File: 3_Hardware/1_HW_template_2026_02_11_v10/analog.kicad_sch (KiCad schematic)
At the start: 8 parts, among them U6 MCP6002-xSN, Y1 ${SIM.PARAMS}

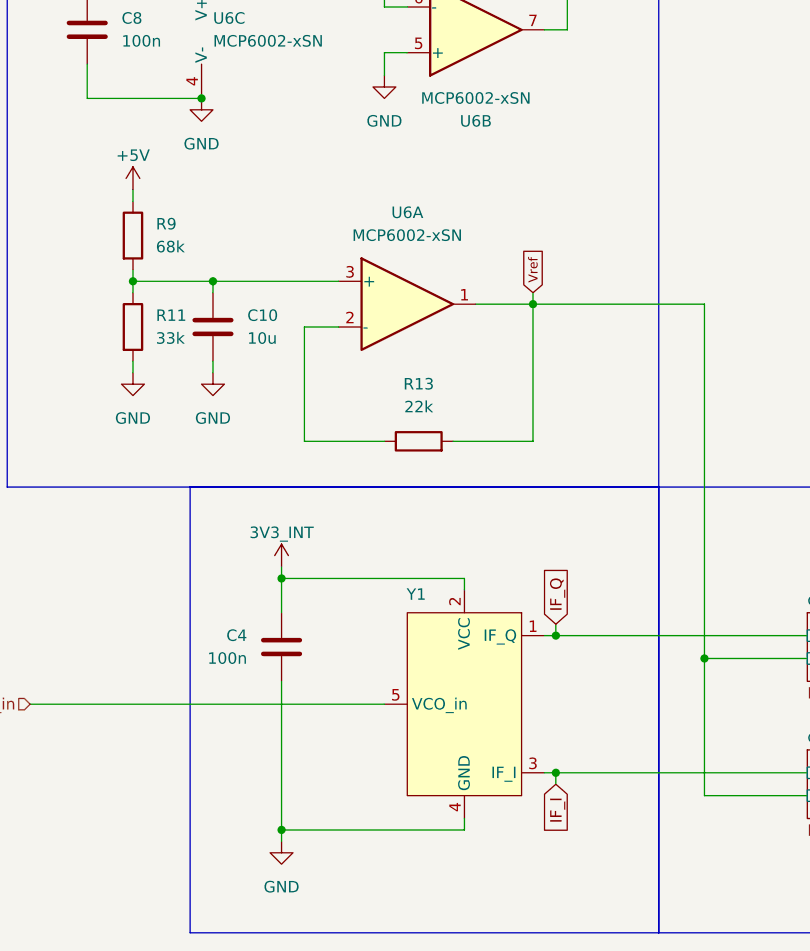
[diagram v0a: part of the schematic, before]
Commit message: added amp filter v5
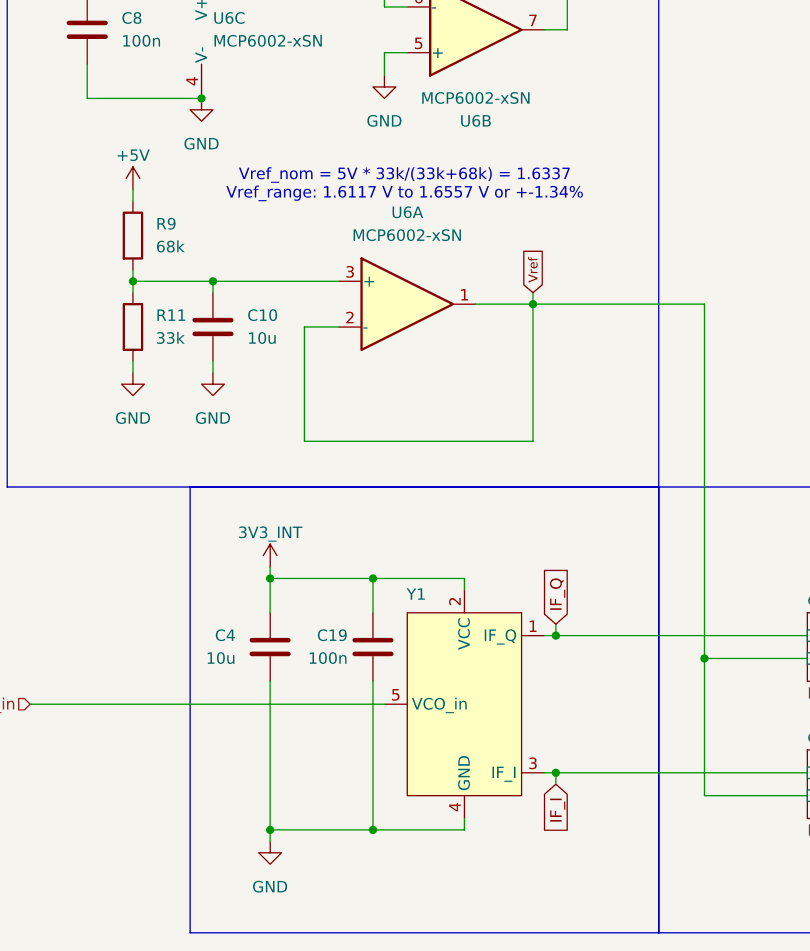
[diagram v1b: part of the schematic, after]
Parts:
- removed R13: 22k, Resistor_SMD:R_0805_2012Metric_Pad1.20x1.40mm_HandSolder, symbol Device:R
- added C19: 100n, Capacitor_SMD:C_0805_2012Metric_Pad1.18x1.45mm_HandSolder, symbol Device:C
- C4: value 100n -> 10u
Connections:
- net 3V3_INT: now also C19.1
- net GND: now also C19.2
- net Vref: now also U6.2 (-)
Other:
- note added: "Vref_nom = 5V * 33k/(33k+68k) = 1.6337 Vref_range: 1.6117 V to 1.6557 V or +-1.34%"
- moved on the sheet: C4
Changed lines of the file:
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@@
+		)
+	)
+	(text "Vref_nom = 5V * 33k/(33k+68k) = 1.6337\nVref_range: 1.6117 V to 1.6557 V or +-1.34%"
+		(exclude_from_sim no)
+		(at 70.866 52.832 0)
+		(effects
+			(font
+				(size 1.27 1.27)
+			)
 		)
 	)
@@
 	)
 	(junction
-		(at 57.15 96.52)
+		(at 67.31 96.52)
 		(diameter 0)
 		(color 0 0 0 0)
@@
 	)
 	(junction
-		(at 57.15 124.46)
+		(at 55.88 124.46)
+		(diameter 0)
+		(color 0 0 0 0)
+	)
+	(junction
+		(at 55.88 96.52)
 		(diameter 0)
 		(color 0 0 0 0)
@@
 	)
 	(junction
+		(at 67.31 124.46)
+		(diameter 0)
+		(color 0 0 0 0)
+	)
+	(junction
 		(at 87.63 118.11)
 		(diameter 0)
@@
 	(wire
 		(pts
+			(xy 55.88 96.52) (xy 67.31 96.52)
+		)
+		(stroke
+			(width 0)
+			(type default)
+		)
+	)
+	(wire
+		(pts
 			(xy 40.64 53.34) (xy 40.64 54.61)
 		)
@@
 	(wire
 		(pts
+			(xy 67.31 107.95) (xy 67.31 124.46)
+		)
+		(stroke
+			(width 0)
+			(type default)
+		)
+	)
+	(wire
+		(pts
 			(xy 88.9 27.94) (xy 88.9 35.56)
 		)
@@
 	(wire
 		(pts
-			(xy 76.2 81.28) (xy 85.09 81.28)
-		)
-		(stroke
-			(width 0)
-			(type default)
-		)
-	)
-	(wire
-		(pts
 			(xy 29.21 110.49) (xy 68.58 110.49)
 		)
@@
 	(wire
 		(pts
+			(xy 55.88 124.46) (xy 67.31 124.46)
+		)
+		(stroke
+			(width 0)
+			(type default)
+		)
+	)
+	(wire
+		(pts
 			(xy 85.09 64.77) (xy 85.09 66.04)
 		)
@@
 	(wire
 		(pts
+			(xy 67.31 96.52) (xy 77.47 96.52)
+		)
+		(stroke
+			(width 0)
+			(type default)
+		)
+	)
+	(wire
+		(pts
 			(xy 71.12 33.02) (xy 68.58 33.02)
 		)
@@
 	(wire
 		(pts
-			(xy 59.69 81.28) (xy 68.58 81.28)
+			(xy 59.69 81.28) (xy 85.09 81.28)
 		)
 		(stroke
@@
 	(wire
 		(pts
+			(xy 67.31 96.52) (xy 67.31 100.33)
+		)
+		(stroke
+			(width 0)
+			(type default)
+		)
+	)
+	(wire
+		(pts
 			(xy 40.64 63.5) (xy 40.64 64.77)
 		)
@@
 	(wire
 		(pts
-			(xy 57.15 124.46) (xy 57.15 125.73)
+			(xy 55.88 124.46) (xy 55.88 125.73)
 		)
 		(stroke
@@
 	(wire
 		(pts
-			(xy 57.15 96.52) (xy 57.15 100.33)
+			(xy 55.88 96.52) (xy 55.88 100.33)
 		)
 		(stroke
@@
 	(wire
 		(pts
-			(xy 57.15 96.52) (xy 77.47 96.52)
-		)
-		(stroke
-			(width 0)
-			(type default)
-		)
-	)
-	(wire
-		(pts
 			(xy 35.56 39.37) (xy 35.56 43.18)
 		)
@@
 	(wire
 		(pts
+			(xy 67.31 124.46) (xy 77.47 124.46)
+		)
+		(stroke
+			(width 0)
+			(type default)
+		)
+	)
+	(wire
+		(pts
 			(xy 104.14 120.65) (xy 104.14 105.41)
 		)
@@
 	(wire
 		(pts
-			(xy 57.15 107.95) (xy 57.15 124.46)
+			(xy 55.88 107.95) (xy 55.88 124.46)
 		)
 		(stroke
@@
 	(wire
 		(pts
-			(xy 57.15 124.46) (xy 77.47 124.46)
-		)
-		(stroke
-			(width 0)
-			(type default)
-		)
-	)
-	(wire
-		(pts
 			(xy 87.63 118.11) (xy 115.57 118.11)
 		)
@@
 	(wire
 		(pts
-			(xy 57.15 95.25) (xy 57.15 96.52)
+			(xy 55.88 95.25) (xy 55.88 96.52)
 		)
 		(stroke
@@
 	)
 	(symbol
-		(lib_id "Device:R")
-		(at 72.39 81.28 90)
+		(lib_id "Device:C")
+		(at 67.31 104.14 0)
+		(mirror y)
 		(unit 1)
 		(exclude_from_sim no)
@@
 		(on_board yes)
 		(dnp no)
-		(fields_autoplaced yes)
-		(property "Reference" "R13"
-			(at 72.39 74.93 90)
-			(effects
-				(font
-					(size 1.27 1.27)
-				)
-			)
-		)
-		(property "Value" "22k"
-			(at 72.39 77.47 90)
-			(effects
-				(font
-					(size 1.27 1.27)
-				)
-			)
-		)
-		(property "Footprint" "Resistor_SMD:R_0805_2012Metric_Pad1.20x1.40mm_HandSolder"
-			(at 72.39 83.058 90)
+		(property "Reference" "C19"
+			(at 64.516 102.87 0)
+			(effects
+				(font
+					(size 1.27 1.27)
+				)
+				(justify left)
+			)
+		)
+		(property "Value" "100n"
+			(at 64.516 105.41 0)
+			(effects
+				(font
+					(size 1.27 1.27)
+				)
+				(justify left)
+			)
+		)
+		(property "Footprint" "Capacitor_SMD:C_0805_2012Metric_Pad1.18x1.45mm_HandSolder"
+			(at 66.3448 107.95 0)
 			(effects
 				(font
@@
 		)
 		(property "Datasheet" "~"
-			(at 72.39 81.28 0)
+			(at 67.31 104.14 0)
 			(effects
 				(font
@@
 		)
 		(property "Description" ""
-			(at 72.39 81.28 0)
+			(at 67.31 104.14 0)
 			(effects
 				(font
@@
 			(project "HW_template"
 				(path "/1f276d59-ad9b-4e70-a842-f3b7e562eb9b/53678366-9d6f-42c1-9420-188f8f258077"
-					(reference "R13")
+					(reference "C19")
 					(unit 1)
 				)
@@
 	(symbol
 		(lib_id "power:GND")
-		(at 57.15 125.73 0)
+		(at 55.88 125.73 0)
 		(mirror y)
 		(unit 1)
@@
 		(fields_autoplaced yes)
 		(property "Reference" "#PWR013"
-			(at 57.15 132.08 0)
+			(at 55.88 132.08 0)
 			(effects
 				(font
@@
 		)
 		(property "Value" "GND"
-			(at 57.15 130.81 0)
+			(at 55.88 130.81 0)
 			(effects
 				(font
@@
 		)
 		(property "Footprint" ""
-			(at 57.15 125.73 0)
+			(at 55.88 125.73 0)
 			(effects
 				(font
@@
 		)
 		(property "Datasheet" ""
-			(at 57.15 125.73 0)
+			(at 55.88 125.73 0)
 			(effects
 				(font
@@
 		)
 		(property "Description" "Power symbol creates a global label with name \"GND\" , ground"
-			(at 57.15 125.73 0)
+			(at 55.88 125.73 0)
 			(effects
 				(font
@@
 	(symbol
 		(lib_id "power:+3V0")
-		(at 57.15 95.25 0)
+		(at 55.88 95.25 0)
 		(mirror y)
 		(unit 1)
@@
 		(dnp no)
 		(property "Reference" "#PWR011"
-			(at 57.15 99.06 0)
+			(at 55.88 99.06 0)
 			(effects
 				(font
@@
 		)
 		(property "Value" "3V3_INT"
-			(at 57.15 91.44 0)
+			(at 55.88 91.44 0)
 			(effects
 				(font
@@
 		)
 		(property "Footprint" ""
-			(at 57.15 95.25 0)
+			(at 55.88 95.25 0)
 			(effects
 				(font
@@
 		)
 		(property "Datasheet" ""
-			(at 57.15 95.25 0)
+			(at 55.88 95.25 0)
 			(effects
 				(font
@@
 		)
 		(property "Description" "Power symbol creates a global label with name \"+3V0\""
-			(at 57.15 95.25 0)
+			(at 55.88 95.25 0)
 			(effects
 				(font
@@
 	(symbol
 		(lib_id "Device:C")
-		(at 57.15 104.14 0)
+		(at 55.88 104.14 0)
 		(mirror y)
 		(unit 1)
@@
 		(fields_autoplaced yes)
 		(property "Reference" "C4"
-			(at 53.34 102.8699 0)
+			(at 52.07 102.8699 0)
 			(effects
 				(font
@@
 			)
 		)
-		(property "Value" "100n"
-			(at 53.34 105.4099 0)
+		(property "Value" "10u"
+			(at 52.07 105.4099 0)
 			(effects
 				(font
@@
 		)
 		(property "Footprint" "Capacitor_SMD:C_0805_2012Metric_Pad1.18x1.45mm_HandSolder"
-			(at 56.1848 107.95 0)
+			(at 54.9148 107.95 0)
 			(effects
 				(font
@@
 		)
 		(property "Datasheet" "~"
-			(at 57.15 104.14 0)
+			(at 55.88 104.14 0)
 			(effects
 				(font
@@
 		)
 		(property "Description" ""
-			(at 57.15 104.14 0)
-			(effects
-				(font
+			(at 55.88 104.14 0)
+			(effects
+				(font

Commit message: finalize main feature
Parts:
- removed unit 2 of U6
- R11: value 33k -> 10k
- R9: value 68k -> 10k
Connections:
- net +5V is gone; now on net 3V3_INT: R9.1
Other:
- note added: "Vref_nom = 3V3 * 10k/(10k+10k) = 1.65 Vref_range: ±16.5 mV ±1%"
- note removed: "Vref_nom = 5V * 33k/(33k+68k) = 1.6337 Vref_range: 1.6117 V to 1.6557 V or +-1.34%"
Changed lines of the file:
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@@
 		)
 	)
-	(text "Vref_nom = 5V * 33k/(33k+68k) = 1.6337\nVref_range: 1.6117 V to 1.6557 V or +-1.34%"
+	(text "Vref_nom = 3V3 * 10k/(10k+10k) = 1.65\nVref_range: ±16.5 mV ±1%"
 		(exclude_from_sim no)
-		(at 70.866 52.832 0)
+		(at 73.152 52.324 0)
 		(effects
 			(font
@@
 	)
 	(junction
-		(at 85.09 66.04)
+		(at 81.28 66.04)
 		(diameter 0)
 		(color 0 0 0 0)
@@
 	(wire
 		(pts
-			(xy 85.09 81.28) (xy 85.09 66.04)
+			(xy 81.28 73.66) (xy 81.28 66.04)
 		)
 		(stroke
@@
 	(wire
 		(pts
-			(xy 88.9 27.94) (xy 88.9 35.56)
-		)
-		(stroke
-			(width 0)
-			(type default)
-		)
-	)
-	(wire
-		(pts
 			(xy 87.63 118.11) (xy 86.36 118.11)
 		)
@@
 	(wire
 		(pts
-			(xy 104.14 66.04) (xy 85.09 66.04)
-		)
-		(stroke
-			(width 0)
-			(type default)
-		)
-	)
-	(wire
-		(pts
-			(xy 68.58 27.94) (xy 88.9 27.94)
+			(xy 104.14 66.04) (xy 81.28 66.04)
 		)
 		(stroke
@@
 	(wire
 		(pts
-			(xy 85.09 64.77) (xy 85.09 66.04)
+			(xy 81.28 64.77) (xy 81.28 66.04)
 		)
 		(stroke
@@
 	(wire
 		(pts
-			(xy 71.12 33.02) (xy 68.58 33.02)
-		)
-		(stroke
-			(width 0)
-			(type default)
-		)
-	)
-	(wire
-		(pts
-			(xy 59.69 81.28) (xy 85.09 81.28)
+			(xy 59.69 73.66) (xy 81.28 73.66)
 		)
 		(stroke
@@
 	(wire
 		(pts
-			(xy 78.74 66.04) (xy 85.09 66.04)
+			(xy 78.74 66.04) (xy 81.28 66.04)
 		)
 		(stroke
@@
 	(wire
 		(pts
-			(xy 68.58 33.02) (xy 68.58 27.94)
-		)
-		(stroke
-			(width 0)
-			(type default)
-		)
-	)
-	(wire
-		(pts
 			(xy 77.47 97.79) (xy 77.47 96.52)
 		)
@@
 	(wire
 		(pts
-			(xy 59.69 68.58) (xy 59.69 81.28)
+			(xy 59.69 68.58) (xy 59.69 73.66)
 		)
 		(stroke
@@
 	(wire
 		(pts
-			(xy 68.58 38.1) (xy 71.12 38.1)
-		)
-		(stroke
-			(width 0)
-			(type default)
-		)
-	)
-	(wire
-		(pts
 			(xy 35.56 39.37) (xy 35.56 43.18)
 		)
@@
 	(wire
 		(pts
-			(xy 86.36 35.56) (xy 88.9 35.56)
-		)
-		(stroke
-			(width 0)
-			(type default)
-		)
-	)
-	(wire
-		(pts
 			(xy 87.63 101.6) (xy 87.63 102.87)
 		)
@@
 		(pts
 			(xy 49.53 72.39) (xy 49.53 73.66)
-		)
-		(stroke
-			(width 0)
-			(type default)
-		)
-	)
-	(wire
-		(pts
-			(xy 68.58 38.1) (xy 68.58 40.64)
 		)
 		(stroke
@@
 	(global_label "Vref"
 		(shape input)
-		(at 85.09 64.77 90)
+		(at 81.28 64.77 90)
 		(fields_autoplaced yes)
 		(effects
@@
 		)
 		(property "Intersheetrefs" "${INTERSHEET_REFS}"
-			(at 85.09 59.5151 90)
+			(at 81.28 59.5151 90)
 			(effects
 				(font
@@
 			)
 			(justify left)
+		)
+	)
+	(symbol
+		(lib_id "power:+3V0")
+		(at 40.64 53.34 0)
+		(unit 1)
+		(exclude_from_sim no)
+		(in_bom yes)
+		(on_board yes)
+		(dnp no)
+		(property "Reference" "#PWR014"
+			(at 40.64 57.15 0)
+			(effects
+				(font
+					(size 1.27 1.27)
+				)
+				(hide yes)
+			)
+		)
+		(property "Value" "3V3_INT"
+			(at 40.64 49.53 0)
+			(effects
+				(font
+					(size 1.27 1.27)
+				)
+			)
+		)
+		(property "Footprint" ""
+			(at 40.64 53.34 0)
+			(effects
+				(font
+					(size 1.27 1.27)
+				)
+				(hide yes)
+			)
+		)
+		(property "Datasheet" ""
+			(at 40.64 53.34 0)
+			(effects
+				(font
+					(size 1.27 1.27)
+				)
+				(hide yes)
+			)
+		)
+		(property "Description" "Power symbol creates a global label with name \"+3V0\""
+			(at 40.64 53.34 0)
+			(effects
+				(font
+					(size 1.27 1.27)
+				)
+				(hide yes)
+			)
+		)
+		(pin "1"
+		)
+		(instances
+			(project "HW_template"
+				(path "/1f276d59-ad9b-4e70-a842-f3b7e562eb9b/53678366-9d6f-42c1-9420-188f8f258077"
+					(reference "#PWR014")
+					(unit 1)
+				)
+			)
 		)
 	)
@@
 	)
 	(symbol
-		(lib_id "power:+5V")
-		(at 40.64 53.34 0)
-		(unit 1)
-		(exclude_from_sim no)
-		(in_bom yes)
-		(on_board yes)
-		(dnp no)
-		(property "Reference" "#PWR021"
-			(at 40.64 57.15 0)
-			(effects
-				(font
-					(size 1.27 1.27)
-				)
-				(hide yes)
-			)
-		)
-		(property "Value" "+5V"
-			(at 40.64 49.53 0)
-			(effects
-				(font
-					(size 1.27 1.27)
-				)
-			)
-		)
-		(property "Footprint" ""
-			(at 40.64 53.34 0)
-			(effects
-				(font
-					(size 1.27 1.27)
-				)
-				(hide yes)
-			)
-		)
-		(property "Datasheet" ""
-			(at 40.64 53.34 0)
-			(effects
-				(font
-					(size 1.27 1.27)
-				)
-				(hide yes)
-			)
-		)
-		(property "Description" "Power symbol creates a global label with name \"+5V\""
-			(at 40.64 53.34 0)
-			(effects
-				(font
-					(size 1.27 1.27)
-				)
-				(hide yes)
-			)
-		)
-		(pin "1"
-		)
-		(instances
-			(project "HW_template"
-				(path "/1f276d59-ad9b-4e70-a842-f3b7e562eb9b/53678366-9d6f-42c1-9420-188f8f258077"
-					(reference "#PWR021")
-					(unit 1)
-				)
-			)
-		)
-	)
-	(symbol
 		(lib_id "Device:R")
 		(at 40.64 68.58 0)
@@
 			)
 		)
-		(property "Value" "33k"
+		(property "Value" "10k"
 			(at 43.18 69.8499 0)
 			(effects
@@
 					(reference "U6")
 					(unit 3)
-				)
-			)
-		)
-	)
-	(symbol
-		(lib_id "Amplifier_Operational:MCP6002-xSN")
-		(at 78.74 35.56 0)
-		(mirror x)
-		(unit 2)
-		(exclude_from_sim no)
-		(in_bom yes)
-		(on_board yes)
-		(dnp no)
-		(property "Reference" "U6"
-			(at 78.74 45.72 0)
-			(effects
-				(font
-					(size 1.27 1.27)
-				)
-			)
-		)
-		(property "Value" "MCP6002-xSN"
-			(at 78.74 43.18 0)
-			(effects
-				(font
-					(size 1.27 1.27)
-				)
-			)
-		)
-		(property "Footprint" "Package_SO:SOIC-8_3.9x4.9mm_P1.27mm"
-			(at 78.74 35.56 0)
-			(effects
-				(font
-					(size 1.27 1.27)
-				)
-				(hide yes)
-			)
-		)
-		(property "Datasheet" "http://ww1.microchip.com/downloads/en/DeviceDoc/21733j.pdf"
-			(at 78.74 35.56 0)
-			(effects
-				(font
-					(size 1.27 1.27)
-				)
-				(hide yes)
-			)
-		)
-		(property "Description" "1MHz, Low-Power Op Amp, SOIC-8"
-			(at 78.74 35.56 0)
-			(effects
-				(font
-					(size 1.27 1.27)
-				)
-				(hide yes)
-			)
-		)
-		(pin "4"
-		)
-		(pin "2"
-		)
-		(pin "6"
-		)
-		(pin "3"
-		)
-		(pin "1"
-		)
-		(pin "7"
-		)
-		(pin "8"
-		)
-		(pin "5"
-		)
-		(instances
-			(project "HW_template"
-				(path "/1f276d59-ad9b-4e70-a842-f3b7e562eb9b/53678366-9d6f-42c1-9420-188f8f258077"
-					(reference "U6")
-					(unit 2)
 				)
 			)
@@
 	)
 	(symbol
-		(lib_id "power:GND")
-		(at 68.58 40.64 0)
-		(unit 1)
-		(exclude_from_sim no)
-		(in_bom yes)
-		(on_board yes)
-		(dnp no)
-		(fields_autoplaced yes)
-		(property "Reference" "#PWR045"
-			(at 68.58 46.99 0)
-			(effects
-				(font
-					(size 1.27 1.27)
-				)
-				(hide yes)
-			)
-		)
-		(property "Value" "GND"
-			(at 68.58 45.72 0)
-			(effects
-				(font
-					(size 1.27 1.27)
-				)
-			)
-		)
-		(property "Footprint" ""
-			(at 68.58 40.64 0)
-			(effects
-				(font
-					(size 1.27 1.27)
-				)
-				(hide yes)
-			)
-		)
-		(property "Datasheet" ""
-			(at 68.58 40.64 0)
-			(effects
-				(font
-					(size 1.27 1.27)
-				)
-				(hide yes)
-			)
-		)
-		(property "Description" "Power symbol creates a global label with name \"GND\" , ground"
-			(at 68.58 40.64 0)
-			(effects
-				(font
-					(size 1.27 1.27)
-				)
-				(hide yes)
-			)
-		)
-		(pin "1"
-		)
-		(instances
-			(project "HW_template"
-				(path "/1f276d59-ad9b-4e70-a842-f3b7e562eb9b/53678366-9d6f-42c1-9420-188f8f258077"
-					(reference "#PWR045")
-					(unit 1)
-				)
-			)
-		)
-	)
-	(symbol
 		(lib_id "Device:C")
 		(at 55.88 104.14 0)
@@
 			)
 		)
-		(property "Value" "68k"
+		(property "Value" "10k"
 			(at 43.18 59.6899 0)
 			(effects

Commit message: layout template
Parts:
- renumbered C4 to C15, C8 to C16, C10 to C17, C19 to C18, R9 to R18, R11 to R19, U6 to U3, Y1 to Y2
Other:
- note added: "Analog Front end Circuitry"
- note added: "K-LC5 Radar sensor"
- note added: "Reference Voltage Generation"
- note added: "Vref_nom = 3V3 * 10k/(10k+10k) = 1.65 Vref_range = ±16.5 mV ±1%"
- note removed: "Vref_nom = 3V3 * 10k/(10k+10k) = 1.65 Vref_range: ±16.5 mV ±1%"
- moved on the sheet: C16, C17, R18, R19, U3A, U3C
